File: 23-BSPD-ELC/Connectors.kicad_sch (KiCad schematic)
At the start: 11 parts, among them J1 Conn_02x08_Counter_Clockwise

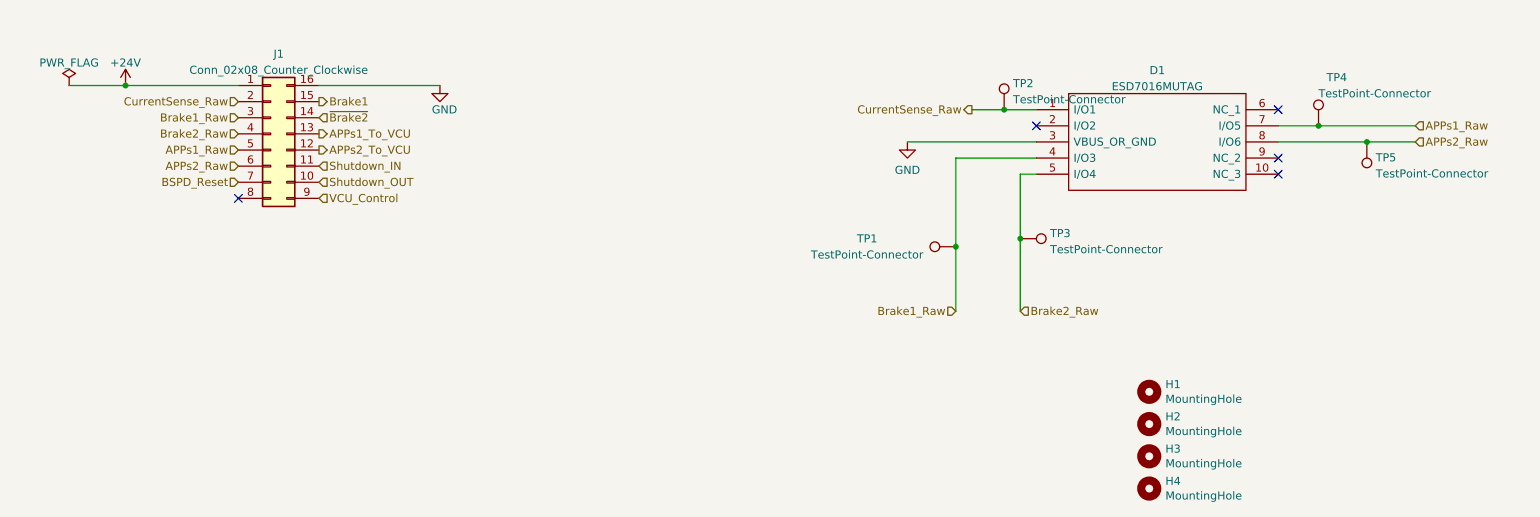
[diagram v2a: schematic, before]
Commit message: Updated pcb layout; Watchdog on board still in progress
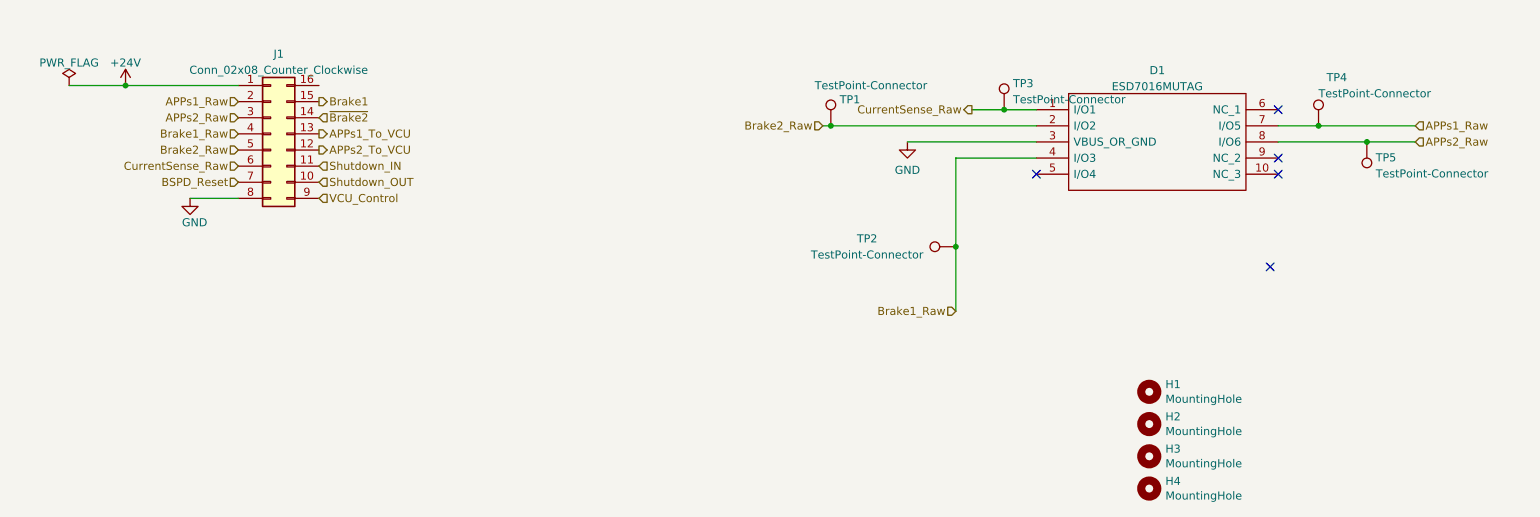
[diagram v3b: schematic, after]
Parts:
- D1: footprint (none) -> Global Libraries:ESD7016MUTAG
- J1: footprint (none) -> Connector_Molex:Molex_Micro-Fit_3.0_43045-1612_2x08_P3.00mm_Vertical
- renumbered TP3 to TP1, TP1 to TP2, TP2 to TP3
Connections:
- net APPs1_Raw: now also J1.2 (Pin_2); no longer J1.5 (Pin_5)
- net APPs2_Raw: now also J1.3 (Pin_3); no longer J1.6 (Pin_6)
- net Brake1_Raw: now also J1.4 (Pin_4); no longer J1.3 (Pin_3)
- net Brake2_Raw: now also D1.2 (I/O2), J1.5 (Pin_5); no longer D1.5 (I/O4), J1.4 (Pin_4)
- net CurrentSense_Raw: now also J1.6 (Pin_6); no longer J1.2 (Pin_2)
- net GND: now also J1.8 (Pin_8); no longer J1.16 (Pin_16)
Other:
- moved on the sheet: TP1
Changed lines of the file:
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@@
   (junction (at 237.49 91.44) (diameter 0) (color 0 0 0 0)
   )
-  (junction (at 190.5 109.22) (diameter 0) (color 0 0 0 0)
-  )
   (junction (at 180.34 110.49) (diameter 0) (color 0 0 0 0)
   )
+  (junction (at 187.96 88.9) (diameter 0) (color 0 0 0 0)
+  )
   (junction (at 49.53 85.09) (diameter 0) (color 0 0 0 0)
   )
   (junction (at 245.11 93.98) (diameter 0) (color 0 0 0 0)
   )
-  (junction (at 187.96 88.9) (diameter 0) (color 0 0 0 0)
-  )
-  (no_connect (at 67.31 102.87))
-  (no_connect (at 193.04 91.44))
+  (junction (at 160.655 91.44) (diameter 0) (color 0 0 0 0)
+  )
+  (no_connect (at 229.87 113.665))
   (no_connect (at 231.14 96.52))
   (no_connect (at 231.14 99.06))
   (no_connect (at 231.14 88.9))
+  (no_connect (at 193.04 99.06))
+  (wire (pts (xy 59.69 102.87) (xy 67.31 102.87))
+    (stroke (width 0) (type default) (color 0 0 0 0))
+  )
   (wire (pts (xy 193.04 96.52) (xy 180.34 96.52))
     (stroke (width 0) (type default) (color 0 0 0 0))
   )
-  (wire (pts (xy 80.01 85.09) (xy 99.06 85.09))
-    (stroke (width 0) (type default) (color 0 0 0 0))
-  )
   (wire (pts (xy 237.49 91.44) (xy 252.73 91.44))
     (stroke (width 0) (type default) (color 0 0 0 0))
   )
+  (wire (pts (xy 159.385 91.44) (xy 160.655 91.44))
+    (stroke (width 0) (type default) (color 0 0 0 0))
+  )
   (wire (pts (xy 187.96 88.9) (xy 193.04 88.9))
     (stroke (width 0) (type default) (color 0 0 0 0))
@@
     (stroke (width 0) (type default) (color 0 0 0 0))
   )
-  (wire (pts (xy 193.04 99.06) (xy 190.5 99.06))
-    (stroke (width 0) (type default) (color 0 0 0 0))
-  )
-  (wire (pts (xy 190.5 99.06) (xy 190.5 109.22))
-    (stroke (width 0) (type default) (color 0 0 0 0))
-  )
   (wire (pts (xy 180.34 96.52) (xy 180.34 110.49))
     (stroke (width 0) (type default) (color 0 0 0 0))
   )
-  (wire (pts (xy 190.5 109.22) (xy 190.5 120.65))
-    (stroke (width 0) (type default) (color 0 0 0 0))
-  )
   (wire (pts (xy 231.14 93.98) (xy 245.11 93.98))
     (stroke (width 0) (type default) (color 0 0 0 0))
@@
     (stroke (width 0) (type default) (color 0 0 0 0))
   )
+  (wire (pts (xy 160.655 91.44) (xy 193.04 91.44))
+    (stroke (width 0) (type default) (color 0 0 0 0))
+  )
   (wire (pts (xy 172.72 93.98) (xy 193.04 93.98))
     (stroke (width 0) (type default) (color 0 0 0 0))
@@
     (stroke (width 0) (type default) (color 0 0 0 0))
   )
-  (hierarchical_label "APPs1_Raw" (shape input) (at 67.31 95.25 180)
+  (hierarchical_label "APPs1_Raw" (shape input) (at 67.31 87.63 180)
     (effects (font (size 1.27 1.27)) (justify right))
   )
@@
     (effects (font (size 1.27 1.27)) (justify left))
   )
-  (hierarchical_label "Brake1_Raw" (shape input) (at 67.31 90.17 180)
+  (hierarchical_label "Brake1_Raw" (shape input) (at 67.31 92.71 180)
     (effects (font (size 1.27 1.27)) (justify right))
   )
@@
     (effects (font (size 1.27 1.27)) (justify left))
   )
-  (hierarchical_label "APPs2_Raw" (shape input) (at 67.31 97.79 180)
-    (effects (font (size 1.27 1.27)) (justify right))
-  )
-  (hierarchical_label "Brake2_Raw" (shape input) (at 190.5 120.65 0)
-    (effects (font (size 1.27 1.27)) (justify left))
+  (hierarchical_label "APPs2_Raw" (shape input) (at 67.31 90.17 180)
+    (effects (font (size 1.27 1.27)) (justify right))
+  )
+  (hierarchical_label "Brake2_Raw" (shape input) (at 159.385 91.44 180)
+    (effects (font (size 1.27 1.27)) (justify right))
   )
   (hierarchical_label "APPs2_Raw" (shape input) (at 252.73 93.98 0)
@@
     (effects (font (size 1.27 1.27)) (justify left))
   )
-  (hierarchical_label "CurrentSense_Raw" (shape input) (at 67.31 87.63 180)
-    (effects (font (size 1.27 1.27)) (justify right))
-  )
-  (hierarchical_label "Brake2_Raw" (shape input) (at 67.31 92.71 180)
-    (effects (font (size 1.27 1.27)) (justify right))
-  )
-  (symbol (lib_id "power:GND") (at 99.06 85.09 0) (mirror y) (unit 1)
-    (in_bom yes) (on_board yes)
-    (property "Reference" "#PWR02" (id 0) (at 99.06 91.44 0)
-      (effects (font (size 1.27 1.27)) hide)
-    )
-    (property "Value" "GND" (id 1) (at 97.79 88.9 0)
+  (hierarchical_label "CurrentSense_Raw" (shape input) (at 67.31 97.79 180)
+    (effects (font (size 1.27 1.27)) (justify right))
+  )
+  (hierarchical_label "Brake2_Raw" (shape input) (at 67.31 95.25 180)
+    (effects (font (size 1.27 1.27)) (justify right))
+  )
+  (symbol (lib_id "power:GND") (at 59.69 102.87 0) (mirror y) (unit 1)
+    (in_bom yes) (on_board yes)
+    (property "Reference" "#PWR02" (id 0) (at 59.69 109.22 0)
+      (effects (font (size 1.27 1.27)) hide)
+    )
+    (property "Value" "GND" (id 1) (at 58.42 106.68 0)
       (effects (font (size 1.27 1.27)) (justify right))
     )
-    (property "Footprint" "" (id 2) (at 99.06 85.09 0)
-      (effects (font (size 1.27 1.27)) hide)
-    )
-    (property "Datasheet" "" (id 3) (at 99.06 85.09 0)
+    (property "Footprint" "" (id 2) (at 59.69 102.87 0)
+      (effects (font (size 1.27 1.27)) hide)
+    )
+    (property "Datasheet" "" (id 3) (at 59.69 102.87 0)
       (effects (font (size 1.27 1.27)) hide)
     )
@@
     )
   )
-  (symbol (lib_id "20-ELC-2-01-R1(Appetizer)-rescue:TestPoint-Connector") (at 190.5 109.22 270) (unit 1)
-    (in_bom yes) (on_board yes) (fields_autoplaced)
-    (property "Reference" "TP3" (id 0) (at 195.199 108.3853 90)
-      (effects (font (size 1.27 1.27)) (justify left))
-    )
-    (property "Value" "TestPoint-Connector" (id 1) (at 195.199 110.9222 90)
-      (effects (font (size 1.27 1.27)) (justify left))
-    )
-    (property "Footprint" "TestPoint:TestPoint_THTPad_D1.0mm_Drill0.5mm" (id 2) (at 190.5 114.3 0)
-      (effects (font (size 1.27 1.27)) hide)
-    )
-    (property "Datasheet" "" (id 3) (at 190.5 114.3 0)
+  (symbol (lib_id "20-ELC-2-01-R1(Appetizer)-rescue:TestPoint-Connector") (at 160.655 91.44 0) (unit 1)
+    (in_bom yes) (on_board yes)
+    (property "Reference" "TP1" (id 0) (at 162.052 87.3033 0)
+      (effects (font (size 1.27 1.27)) (justify left))
+    )
+    (property "Value" "TestPoint-Connector" (id 1) (at 158.115 85.09 0)
+      (effects (font (size 1.27 1.27)) (justify left))
+    )
+    (property "Footprint" "TestPoint:TestPoint_THTPad_D1.0mm_Drill0.5mm" (id 2) (at 165.735 91.44 0)
+      (effects (font (size 1.27 1.27)) hide)
+    )
+    (property "Datasheet" "" (id 3) (at 165.735 91.44 0)
       (effects (font (size 1.27 1.27)) hide)
     )
@@
     (property "Reference" "J1" (id 0) (at 73.66 80.1202 0))
     (property "Value" "Conn_02x08_Counter_Clockwise" (id 1) (at 73.66 82.6571 0))
-    (property "Footprint" "" (id 2) (at 72.39 92.71 0)
+    (property "Footprint" "Connector_Molex:Molex_Micro-Fit_3.0_43045-1612_2x08_P3.00mm_Vertical" (id 2) (at 72.39 92.71 0)
       (effects (font (size 1.27 1.27)) hide)
     )
@@
   (symbol (lib_id "20-ELC-2-01-R1(Appetizer)-rescue:TestPoint-Connector") (at 180.34 110.49 90) (unit 1)
     (in_bom yes) (on_board yes)
-    (property "Reference" "TP1" (id 0) (at 166.37 109.22 90))
+    (property "Reference" "TP2" (id 0) (at 166.37 109.22 90))
     (property "Value" "TestPoint-Connector" (id 1) (at 166.37 111.76 90))
     (property "Footprint" "TestPoint:TestPoint_THTPad_D1.0mm_Drill0.5mm" (id 2) (at 180.34 105.41 0)
@@
   (symbol (lib_id "20-ELC-2-01-R1(Appetizer)-rescue:TestPoint-Connector") (at 187.96 88.9 0) (unit 1)
     (in_bom yes) (on_board yes) (fields_autoplaced)
-    (property "Reference" "TP2" (id 0) (at 189.357 84.7633 0)
+    (property "Reference" "TP3" (id 0) (at 189.357 84.7633 0)
       (effects (font (size 1.27 1.27)) (justify left))
     )
@@
     (pin "1")
   )
-  (symbol (lib_id "LHR 2023 Schematic Library:ESD7016MUTAG") (at 193.04 88.9 0) (unit 1)
+  (symbol (lib_name "ESD7016MUTAG_1") (lib_id "LHR 2023 Schematic Library:ESD7016MUTAG") (at 193.04 88.9 0) (unit 1)
     (in_bom yes) (on_board yes) (fields_autoplaced)
     (property "Reference" "D1" (id 0) (at 212.09 82.711 0))
     (property "Value" "ESD7016MUTAG" (id 1) (at 212.09 85.2479 0))
-    (property "Footprint" "" (id 2) (at 227.33 86.36 0)
+    (property "Footprint" "Global Libraries:ESD7016MUTAG" (id 2) (at 227.33 86.36 0)
       (effects (font (size 1.27 1.27)) (justify left) hide)
     )

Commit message: BSPD layout
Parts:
- removed J1: Conn_02x08_Counter_Clockwise, Connector_Molex:Molex_Micro-Fit_3.0_43045-1612_2x08_P3.00mm_Vertical, symbol Connector_Generic:Conn_02x08_Counter_Clockwise
- added J1: Conn_02x10_Counter_Clockwise, Connector_Molex:Molex_Micro-Fit_3.0_43045-2012_2x10_P3.00mm_Vertical, symbol Connector_Generic:Conn_02x10_Counter_Clockwise
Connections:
- net +24V: now also J1.1 (Pin_1)
- net APPs1_Raw: now also J1.2 (Pin_2)
- net APPs1_To_VCU: now also J1.18 (Pin_18)
- net APPs2_Raw: now also J1.3 (Pin_3)
- net APPs2_To_VCU: now also J1.17 (Pin_17)
- net BSPD_Reset: now also J1.7 (Pin_7)
- net Brake1: now also J1.20 (Pin_20)
- net Brake1_Raw: now also J1.4 (Pin_4)
- net Brake2_Raw: now also J1.5 (Pin_5)
- net CurrentSense_Raw: now also J1.6 (Pin_6)
- net GND: now also J1.8 (Pin_8)
- net Shutdown_IN: now also J1.16 (Pin_16)
- net Shutdown_OUT: now also J1.15 (Pin_15)
- net VCU_Control: now also J1.14 (Pin_14)
- net ~{Brake2}: now also J1.19 (Pin_19)
- new net CANH: J1.12 (Pin_12)
- new net CANL: J1.13 (Pin_13)
- no-connect marks 5 -> 8
